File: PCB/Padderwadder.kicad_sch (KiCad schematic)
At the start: 5 parts, among them J1 OLED_128x32, SW3 SW_Push, SW4 SW_Push, SW5 SW_Push, U1 MOUDLE-SEEEDUINO-XIAO

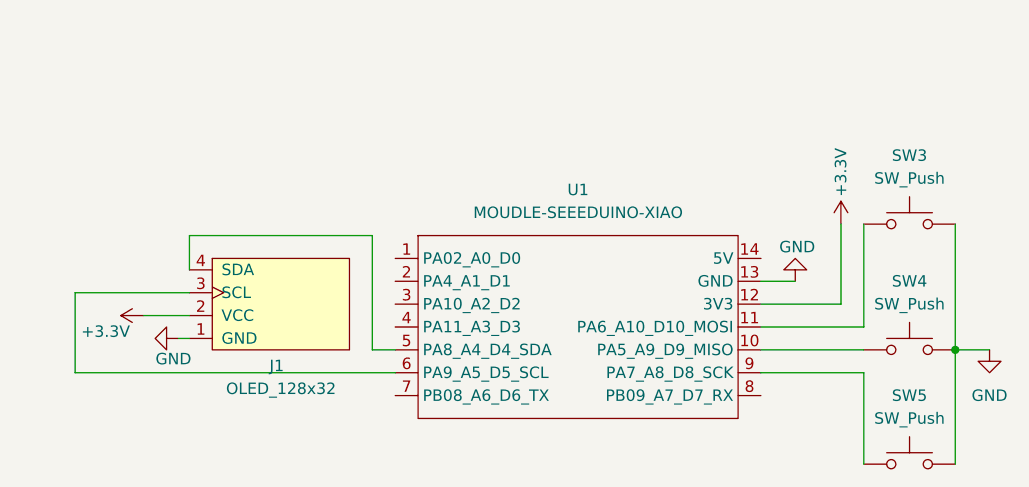
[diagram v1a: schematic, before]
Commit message: Addition of rotary encoder
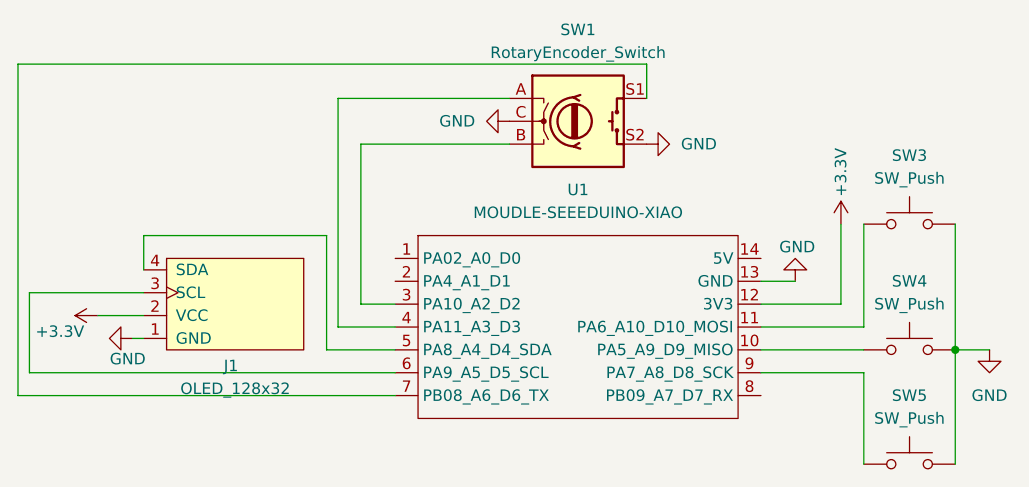
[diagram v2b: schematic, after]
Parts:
- added SW1: RotaryEncoder_Switch, Rotary_Encoder:RotaryEncoder_Alps_EC11E-Switch_Vertical_H20mm, symbol Device:RotaryEncoder_Switch
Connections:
- net GND: now also SW1.C, SW1.S2
- net at U1.3 (PA10_A2_D2): now also SW1.B
- net at U1.4 (PA11_A3_D3): now also SW1.A
- net at U1.7 (PB08_A6_D6_TX): now also SW1.S1
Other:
- moved on the sheet: J1
